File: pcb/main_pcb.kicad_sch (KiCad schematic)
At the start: 47 parts, among them J1 Conn_01x06_Socket, J4 USB_C_Receptacle_USB2.0, Q1 Si2323DS, SW1 Pair, SW2 Reset, SW3 Boot, U1 ESP32-H2-MINI-1, U2 LM5165Y, Y1 32.768KHz

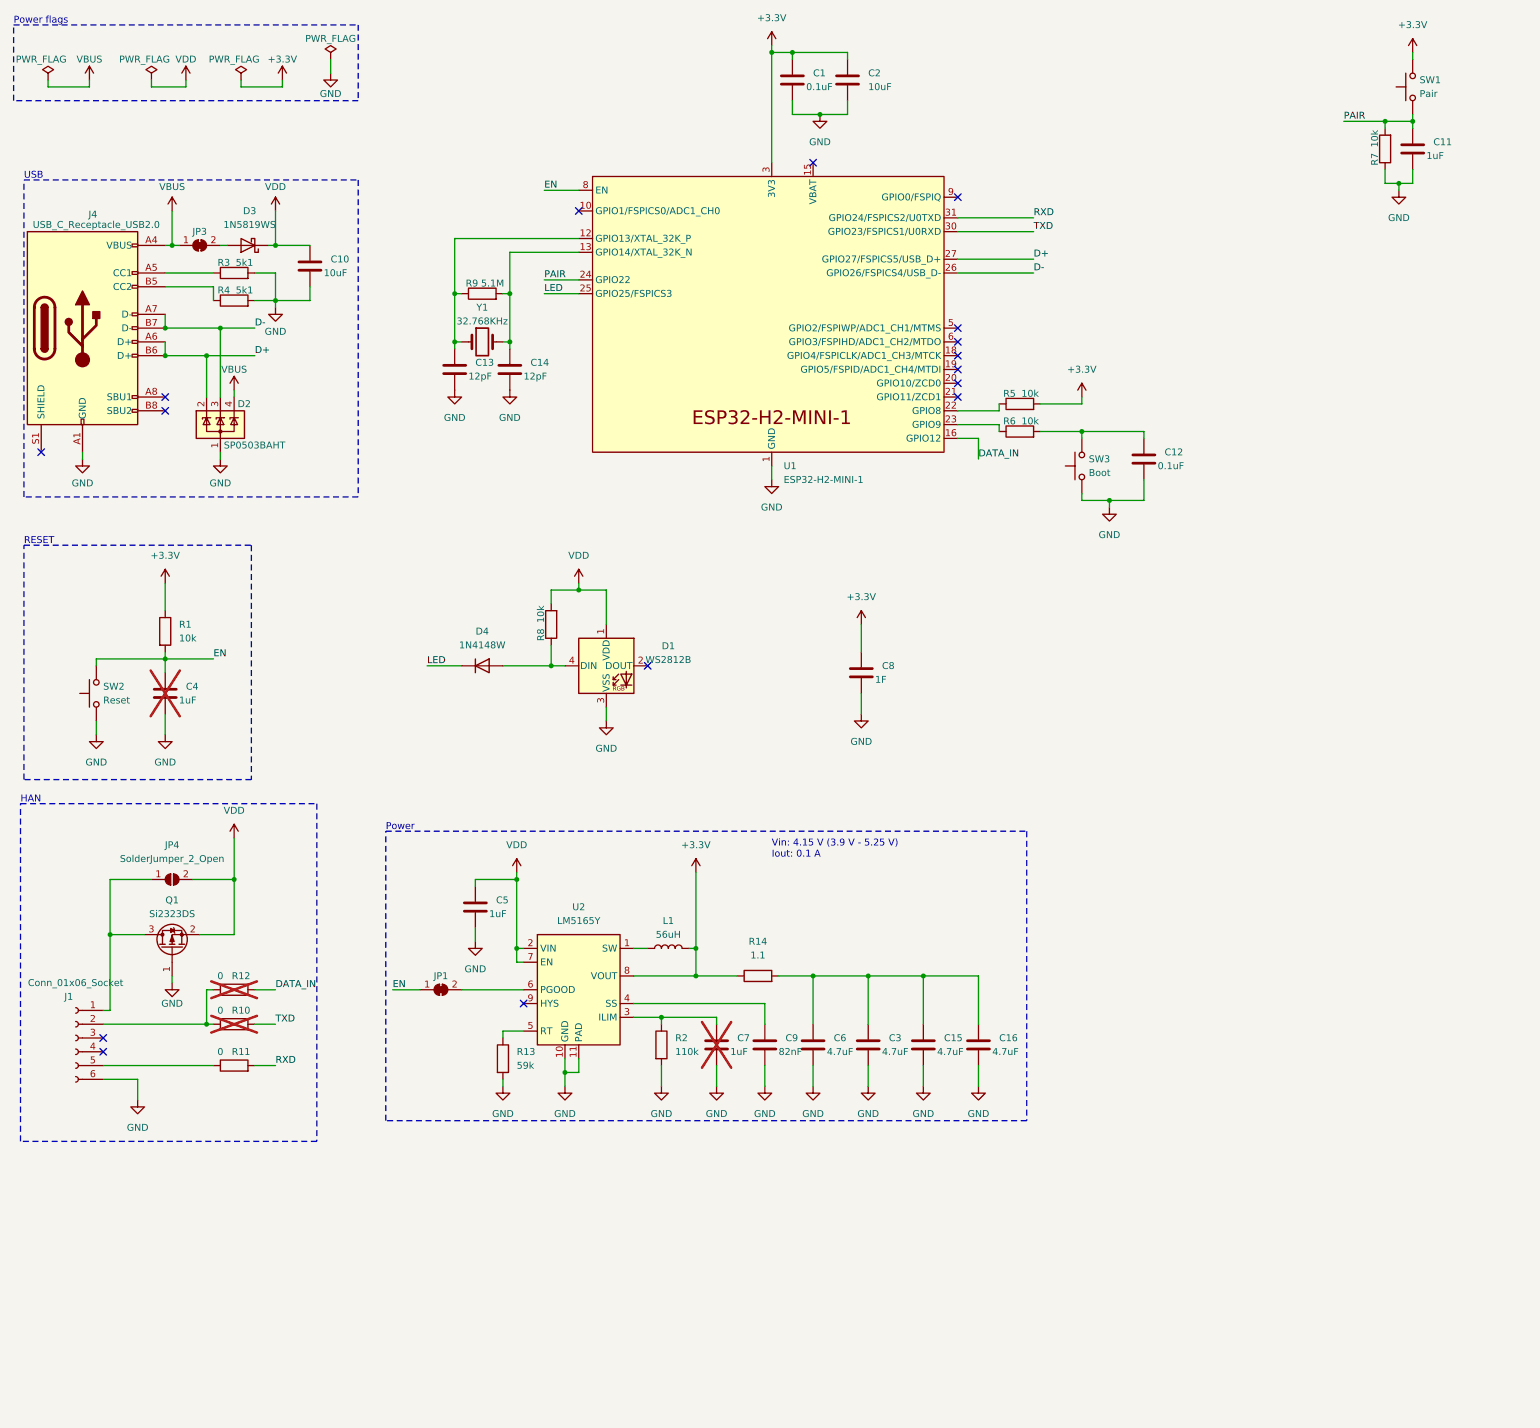
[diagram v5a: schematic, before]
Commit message: Add test points
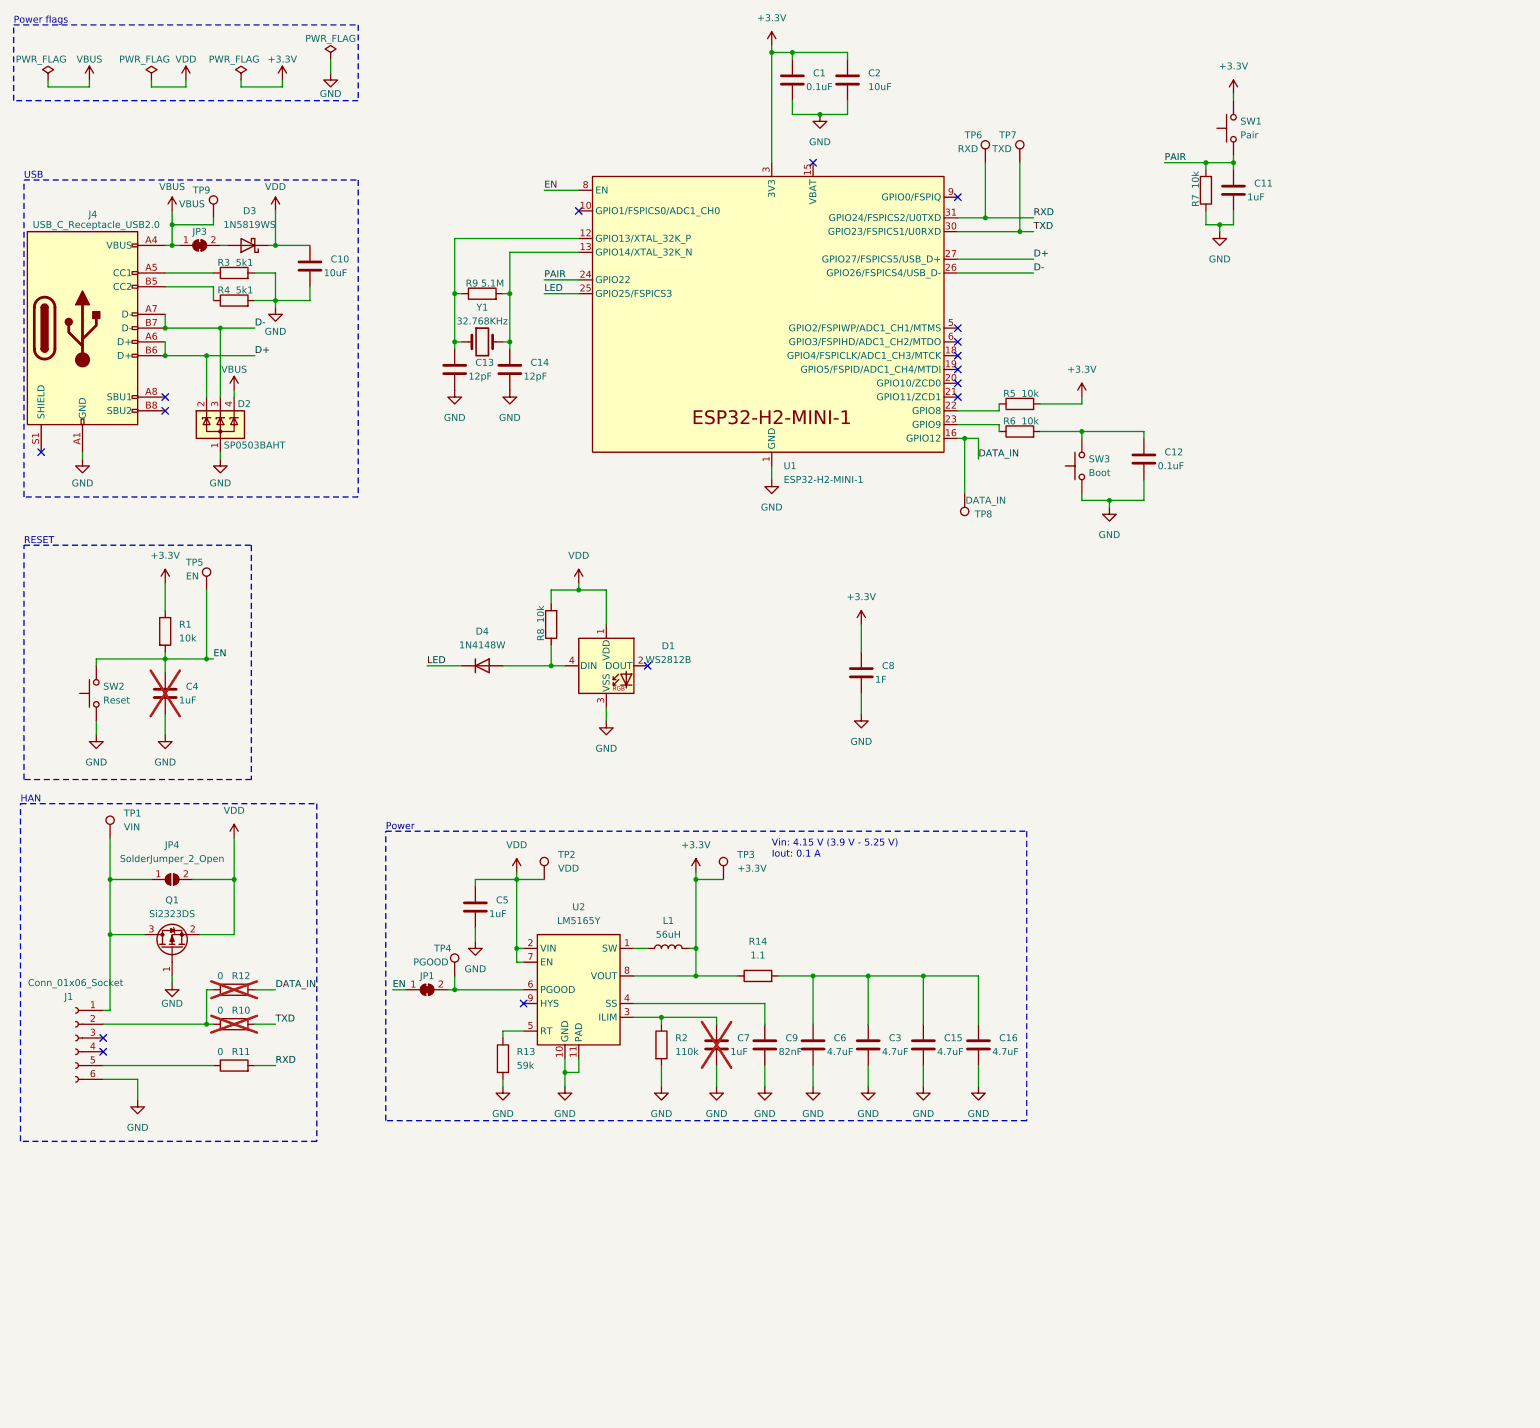
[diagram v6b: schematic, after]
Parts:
- added TP1: VIN, TestPoint:TestPoint_THTPad_D1.5mm_Drill0.7mm, symbol Connector:TestPoint
- added TP2: VDD, TestPoint:TestPoint_THTPad_D2.0mm_Drill1.0mm, symbol Connector:TestPoint
- added TP3: +3.3V, TestPoint:TestPoint_THTPad_D2.0mm_Drill1.0mm, symbol Connector:TestPoint
- added TP4: PGOOD, TestPoint:TestPoint_THTPad_D1.5mm_Drill0.7mm, symbol Connector:TestPoint
- added TP5: EN, TestPoint:TestPoint_THTPad_D1.5mm_Drill0.7mm, symbol Connector:TestPoint
- added TP6: RXD, TestPoint:TestPoint_THTPad_D1.5mm_Drill0.7mm, symbol Connector:TestPoint
- added TP7: TXD, TestPoint:TestPoint_THTPad_D1.5mm_Drill0.7mm, symbol Connector:TestPoint
- added TP8: DATA_IN, TestPoint:TestPoint_THTPad_D1.5mm_Drill0.7mm, symbol Connector:TestPoint
- added TP9: VBUS, TestPoint:TestPoint_THTPad_D1.5mm_Drill0.7mm, symbol Connector:TestPoint
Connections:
- net +3.3V: now also TP3.1
- net DATA_IN: now also TP8.1
- net EN: now also TP5.1
- net RXD: now also TP6.1
- net TXD: now also TP7.1
- net VBUS: now also TP9.1
- net VDD: now also TP2.1
- net at J1.1 (Pin_1), JP4.1 (A), Q1.3 (D): now also TP1.1
- net at JP1.2 (B), U2.6 (PGOOD): now also TP4.1
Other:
- moved on the sheet: C11, JP1, R7, SW1

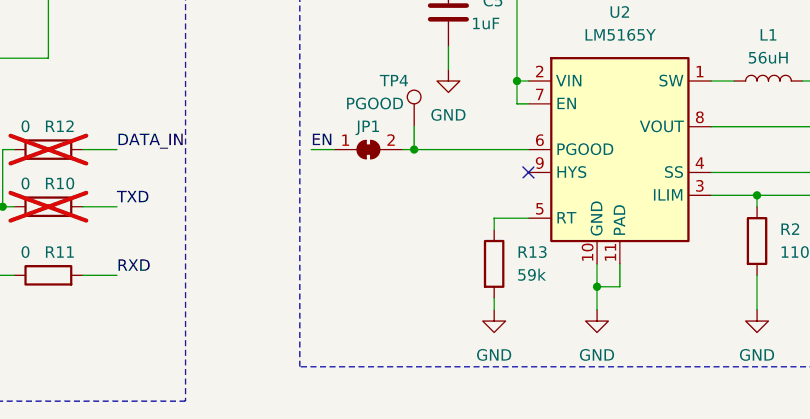
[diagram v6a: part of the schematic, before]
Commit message: Add GND test point
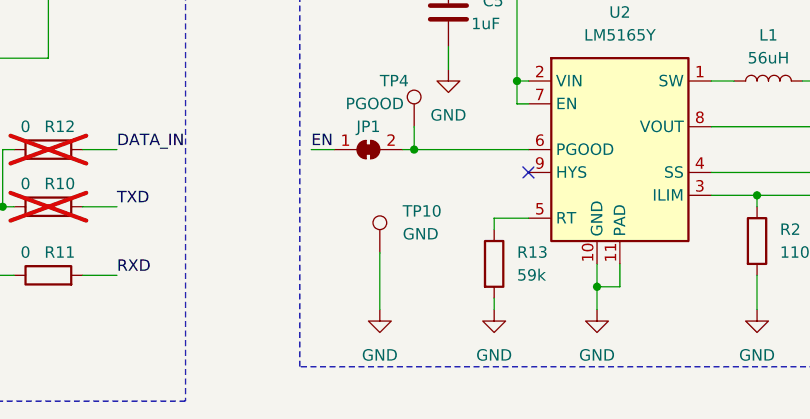
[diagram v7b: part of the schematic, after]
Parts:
- added TP10: GND, TestPoint:TestPoint_THTPad_D2.0mm_Drill1.0mm, symbol Connector:TestPoint
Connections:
- net GND: now also TP10.1
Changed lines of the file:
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@@
+    (stroke (width 0) (type default))
+  )
+  (wire (pts (xy 97.79 212.09) (xy 97.79 218.44))
     (stroke (width 0) (type default))
   )
@@
     )
   )
+  (symbol (lib_id "Connector:TestPoint") (at 97.79 212.09 0) (unit 1)
+    (in_bom yes) (on_board yes) (dnp no) (fields_autoplaced)
+    (property "Reference" "TP10" (at 100.33 207.518 0)
+      (effects (font (size 1.27 1.27)) (justify left))
+    )
+    (property "Value" "GND" (at 100.33 210.058 0) (do_not_autoplace)
+      (effects (font (size 1.27 1.27)) (justify left))
+    )
+    (property "Footprint" "TestPoint:TestPoint_THTPad_D2.0mm_Drill1.0mm" (at 102.87 212.09 0)
+      (effects (font (size 1.27 1.27)) hide)
+    )
+    (property "Datasheet" "~" (at 102.87 212.09 0)
+      (effects (font (size 1.27 1.27)) hide)
+    )
+    (pin "1")
+    (instances
+      (project "main_pcb"
+        (path "/6204b7c2-8814-41ee-9243-5078f55f08d4"
+          (reference "TP10") (unit 1)
+        )
+      )
+    )
+  )
   (symbol (lib_id "Connector:TestPoint") (at 38.1 172.72 0) (unit 1)
     (in_bom yes) (on_board yes) (dnp no) (fields_autoplaced)
@@
         )
       )
+    )
+  )
+  (symbol (lib_id "power:GND") (at 97.79 218.44 0) (unit 1)
+    (in_bom yes) (on_board yes) (dnp no) (fields_autoplaced)
+    (property "Reference" "#PWR042" (at 97.79 224.79 0)
+      (effects (font (size 1.27 1.27)) hide)
+    )
+    (property "Value" "GND" (at 97.79 223.52 0)
+      (effects (font (size 1.27 1.27)))
+    )
+    (property "Footprint" "" (at 97.79 218.44 0)
+      (effects (font (size 1.27 1.27)) hide)
+    )
+    (property "Datasheet" "" (at 97.79 218.44 0)
+      (effects (font (size 1.27 1.27)) hide)
+    )
+    (pin "1")
+    (instances
+      (project "main_pcb"
+        (path "/6204b7c2-8814-41ee-9243-5078f55f08d4"
+          (reference "#PWR042") (unit 1)
+        )
+      )
